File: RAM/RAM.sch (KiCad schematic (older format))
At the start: 31 parts, among them J1 Conn_01x08_Male, J2 Conn_01x08_Male, J3 Conn_01x08_Male, J4 Conn_01x05_Male, J5 Conn_01x08_Male, Q1 IRLML5203, U1 74LS283, U2 CY62256-70PC, U3 74LS283, U4 74LS283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

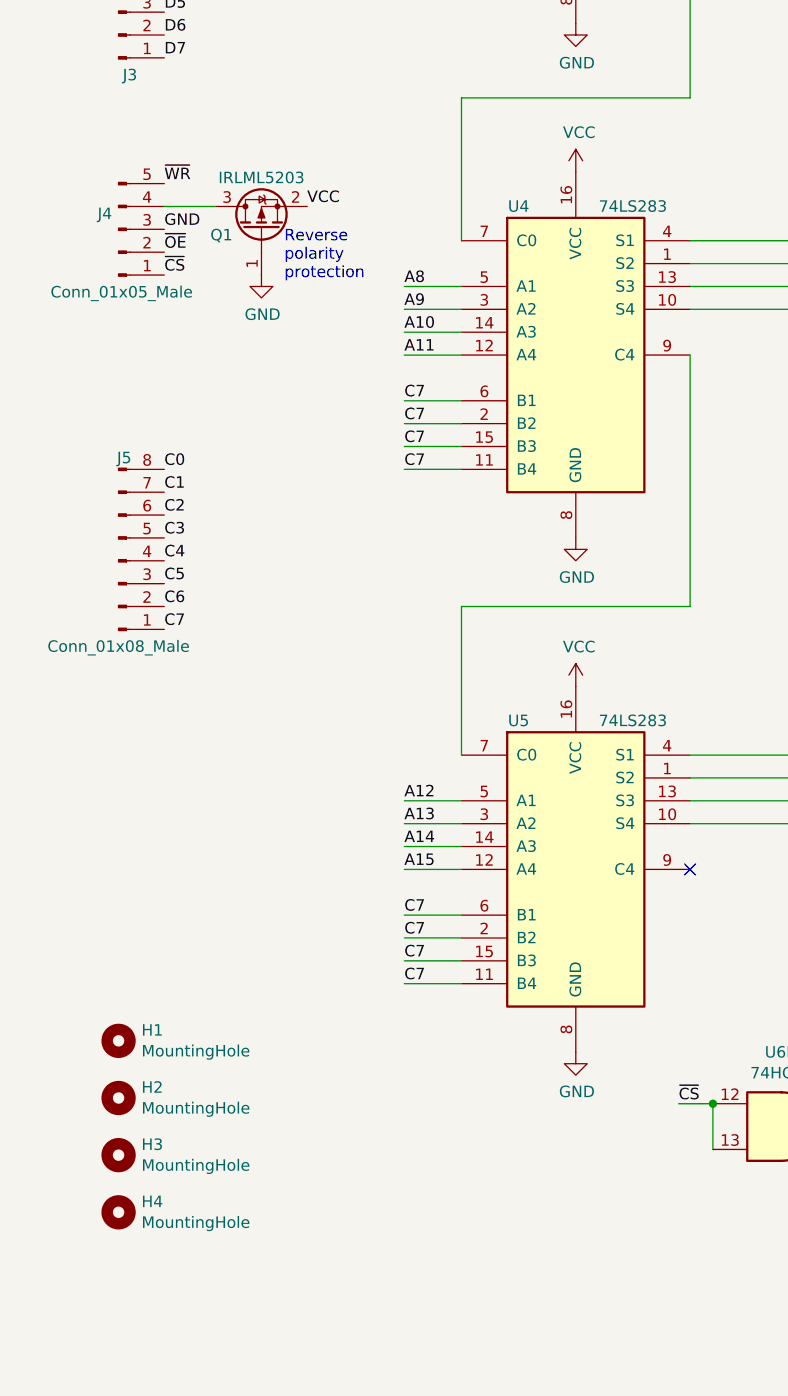
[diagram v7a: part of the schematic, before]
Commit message: Polishing RAM
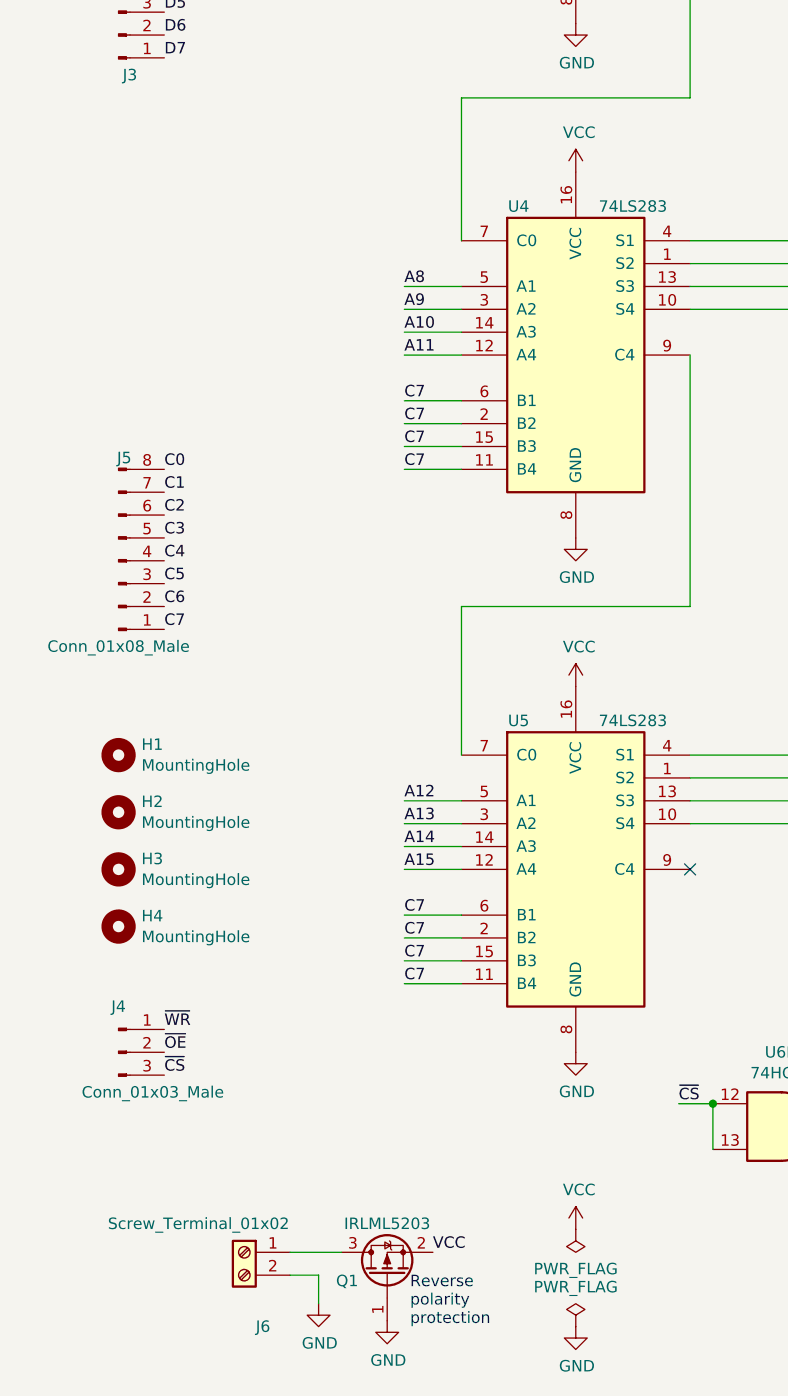
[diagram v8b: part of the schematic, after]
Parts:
- removed J4: Conn_01x05_Male, Connector_PinHeader_2.54mm:PinHeader_1x05_P2.54mm_Vertical, symbol Connector:Conn_01x05_Male
- added J4: Conn_01x03_Male, Connector_PinHeader_2.54mm:PinHeader_1x03_P2.54mm_Vertical, symbol Connector:Conn_01x03_Male
- added J6: Screw_Terminal_01x02, TerminalBlock_Phoenix:TerminalBlock_Phoenix_MKDS-1,5-2_1x02_P5.00mm_Horizontal, symbol Connector:Screw_Terminal_01x02
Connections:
- net GND: now also J6.2 (Pin_2)
- net ~CS: now also J4.3 (Pin_3)
- net ~OE: now also J4.2 (Pin_2)
- net ~WR: now also J4.1 (Pin_1)
- net at Q1.3 (D): now also J6.1 (Pin_1)
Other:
- moved on the sheet: H1, H2, H3, H4, Q1
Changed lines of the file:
@@
 	4200 2650 5000 2650
 NoConn ~ 3250 8500
-Text Label 950  5800 0    50   ~ 0
+Text Label 950  9300 0    50   ~ 0
 ~OE
-Text Label 950  5700 0    50   ~ 0
-GND
-Text Label 1575 5600 0    50   ~ 0
+Text Label 2125 10175 0    50   ~ 0
 VCC
-Text Label 950  5500 0    50   ~ 0
+Text Label 950  9200 0    50   ~ 0
 ~WR
-$Comp
-L Connector:Conn_01x05_Male J4
-U 1 1 63DBE3C2
-P 750 5700
-F 0 "J4" H 722 5632 50  0000 R CNN
-F 1 "Conn_01x05_Male" H 1075 5975 50  0000 R CNN
-F 2 "Connector_PinHeader_2.54mm:PinHeader_1x05_P2.54mm_Vertical" H 750 5700 50  0001 C CNN
-F 3 "~" H 750 5700 50  0001 C CNN
-	1    750  5700
-	1    0    0    1
-$EndComp
-Text Label 950  5900 0    50   ~ 0
+Text Label 950  9400 0    50   ~ 0
 ~CS
 Text Label 6000 2450 0    50   ~ 0
@@
 L Mechanical:MountingHole H1
 U 1 1 64922E67
-P 750 9250
-F 0 "H1" H 850 9296 50  0000 L CNN
-F 1 "MountingHole" H 850 9205 50  0000 L CNN
-F 2 "MountingHole:MountingHole_3.2mm_M3" H 750 9250 50  0001 C CNN
-F 3 "~" H 750 9250 50  0001 C CNN
-	1    750  9250
+P 750 8000
+F 0 "H1" H 850 8046 50  0000 L CNN
+F 1 "MountingHole" H 850 7955 50  0000 L CNN
+F 2 "MountingHole:MountingHole_3.2mm_M3" H 750 8000 50  0001 C CNN
+F 3 "~" H 750 8000 50  0001 C CNN
+	1    750  8000
 	1    0    0    -1
 $EndComp
@@
 L Mechanical:MountingHole H2
 U 1 1 64923BB4
-P 750 9500
-F 0 "H2" H 850 9546 50  0000 L CNN
-F 1 "MountingHole" H 850 9455 50  0000 L CNN
-F 2 "MountingHole:MountingHole_3.2mm_M3" H 750 9500 50  0001 C CNN
-F 3 "~" H 750 9500 50  0001 C CNN
-	1    750  9500
+P 750 8250
+F 0 "H2" H 850 8296 50  0000 L CNN
+F 1 "MountingHole" H 850 8205 50  0000 L CNN
+F 2 "MountingHole:MountingHole_3.2mm_M3" H 750 8250 50  0001 C CNN
+F 3 "~" H 750 8250 50  0001 C CNN
+	1    750  8250
 	1    0    0    -1
 $EndComp
@@
 L Mechanical:MountingHole H3
 U 1 1 64924557
-P 750 9750
-F 0 "H3" H 850 9796 50  0000 L CNN
-F 1 "MountingHole" H 850 9705 50  0000 L CNN
-F 2 "MountingHole:MountingHole_3.2mm_M3" H 750 9750 50  0001 C CNN
-F 3 "~" H 750 9750 50  0001 C CNN
-	1    750  9750
+P 750 8500
+F 0 "H3" H 850 8546 50  0000 L CNN
+F 1 "MountingHole" H 850 8455 50  0000 L CNN
+F 2 "MountingHole:MountingHole_3.2mm_M3" H 750 8500 50  0001 C CNN
+F 3 "~" H 750 8500 50  0001 C CNN
+	1    750  8500
 	1    0    0    -1
 $EndComp
@@
 L Mechanical:MountingHole H4
 U 1 1 64924E63
-P 750 10000
-F 0 "H4" H 850 10046 50  0000 L CNN
-F 1 "MountingHole" H 850 9955 50  0000 L CNN
-F 2 "MountingHole:MountingHole_3.2mm_M3" H 750 10000 50  0001 C CNN
-F 3 "~" H 750 10000 50  0001 C CNN
-	1    750  10000
+P 750 8750
+F 0 "H4" H 850 8796 50  0000 L CNN
+F 1 "MountingHole" H 850 8705 50  0000 L CNN
+F 2 "MountingHole:MountingHole_3.2mm_M3" H 750 8750 50  0001 C CNN
+F 3 "~" H 750 8750 50  0001 C CNN
+	1    750  8750
 	1    0    0    -1
 $EndComp
@@
 L Transistor_FET:IRLML5203 Q1
 U 1 1 64C0CC9D
-P 1375 5700
-F 0 "Q1" V 1350 5875 50  0000 C CNN
-F 1 "IRLML5203" V 1600 5700 50  0000 C CNN
-F 2 "Package_TO_SOT_SMD:SOT-23" H 1575 5625 50  0001 L CIN
-F 3 "https://www.infineon.com/dgdl/irlml5203pbf.pdf?fileId=5546d462533600a40153566868da261d" H 1375 5700 50  0001 L CNN
-	1    1375 5700
+P 1925 10275
+F 0 "Q1" V 1900 10450 50  0000 C CNN
+F 1 "IRLML5203" V 2150 10275 50  0000 C CNN
+F 2 "Package_TO_SOT_SMD:SOT-23" H 2125 10200 50  0001 L CIN
+F 3 "https://www.infineon.com/dgdl/irlml5203pbf.pdf?fileId=5546d462533600a40153566868da261d" H 1925 10275 50  0001 L CNN
+	1    1925 10275
 	0    -1   -1   0
 $EndComp
@@
 L power:GND #PWR0102
 U 1 1 64C0F060
-P 1375 5900
-F 0 "#PWR0102" H 1375 5650 50  0001 C CNN
-F 1 "GND" H 1380 5727 50  0000 C CNN
-F 2 "" H 1375 5900 50  0001 C CNN
-F 3 "" H 1375 5900 50  0001 C CNN
-	1    1375 5900
-	1    0    0    -1
-$EndComp
-Wire Wire Line
-	950  5600 1175 5600
-Text Notes 1475 5925 0    50   ~ 0
+P 1925 10475
+F 0 "#PWR0102" H 1925 10225 50  0001 C CNN
+F 1 "GND" H 1930 10302 50  0000 C CNN
+F 2 "" H 1925 10475 50  0001 C CNN
+F 3 "" H 1925 10475 50  0001 C CNN
+	1    1925 10475
+	1    0    0    -1
+$EndComp
+Wire Wire Line
+	1500 10175 1725 10175
+Text Notes 2025 10500 0    50   ~ 0
 Reverse\npolarity\nprotection
+$Comp
+L Connector:Screw_Terminal_01x02 J6
+U 1 1 669F52FC
+P 1300 10175
+F 0 "J6" H 1218 9850 50  0000 C CNN
+F 1 "Screw_Terminal_01x02" H 1500 10300 50  0000 C CNN
+F 2 "TerminalBlock_Phoenix:TerminalBlock_Phoenix_MKDS-1,5-2_1x02_P5.00mm_Horizontal" H 1300 10175 50  0001 C CNN
+F 3 "~" H 1300 10175 50  0001 C CNN
+	1    1300 10175
+	-1   0    0    -1
+$EndComp
+$Comp
+L power:GND #PWR027
+U 1 1 66A2007B
+P 1625 10400
+F 0 "#PWR027" H 1625 10150 50  0001 C CNN
+F 1 "GND" H 1630 10227 50  0000 C CNN
+F 2 "" H 1625 10400 50  0001 C CNN
+F 3 "" H 1625 10400 50  0001 C CNN
+	1    1625 10400
+	1    0    0    -1
+$EndComp
+Wire Wire Line
+	1500 10275 1625 10275
+Wire Wire Line
+	1625 10275 1625 10400
+$Comp
+L power:PWR_FLAG #FLG03
+U 1 1 66A26073
+P 2750 10075
+F 0 "#FLG03" H 2750 10150 50  0001 C CNN
+F 1 "PWR_FLAG" H 2750 10248 50  0000 C CNN
+F 2 "" H 2750 10075 50  0001 C CNN
+F 3 "~" H 2750 10075 50  0001 C CNN
+	1    2750 10075
+	-1   0    0    1
+$EndComp
+$Comp
+L power:PWR_FLAG #FLG04
+U 1 1 66A26A72
+P 2750 10500
+F 0 "#FLG04" H 2750 10575 50  0001 C CNN
+F 1 "PWR_FLAG" H 2750 10673 50  0000 C CNN
+F 2 "" H 2750 10500 50  0001 C CNN
+F 3 "~" H 2750 10500 50  0001 C CNN
+	1    2750 10500
+	1    0    0    -1
+$EndComp
+$Comp
+L power:GND #PWR029
+U 1 1 66A36050
+P 2750 10500
+F 0 "#PWR029" H 2750 10250 50  0001 C CNN
+F 1 "GND" H 2755 10327 50  0000 C CNN
+F 2 "" H 2750 10500 50  0001 C CNN
+F 3 "" H 2750 10500 50  0001 C CNN
+	1    2750 10500
+	1    0    0    -1
+$EndComp
+$Comp
+L power:VCC #PWR028
+U 1 1 66A37595
+P 2750 10075
+F 0 "#PWR028" H 2750 9925 50  0001 C CNN
+F 1 "VCC" H 2765 10248 50  0000 C CNN
+F 2 "" H 2750 10075 50  0001 C CNN
+F 3 "" H 2750 10075 50  0001 C CNN
+	1    2750 10075
+	1    0    0    -1
+$EndComp
+$Comp
+L Connector:Conn_01x03_Male J4
+U 1 1 66A40C29
+P 750 9300
+F 0 "J4" H 750 9500 50  0000 C CNN
+F 1 "Conn_01x03_Male" H 900 9125 50  0000 C CNN
+F 2 "Connector_PinHeader_2.54mm:PinHeader_1x03_P2.54mm_Vertical" H 750 9300 50  0001 C CNN
+F 3 "~" H 750 9300 50  0001 C CNN
+	1    750  9300
+	1    0    0    -1
+$EndComp
 $EndSCHEMATC
